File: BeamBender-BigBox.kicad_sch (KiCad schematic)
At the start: 124 parts, among them CN1 A4000-CN621-36, CN2 A4000-CN622-54, J1 HDMI, J2 JTAG, J3 JTAG_Pogo, J4 EXT_BUTTONS, SW1 MENU, SW2 UP, SW3 DOWN, U1 Colorlight-i5-v7.0, U2 TLV76133DCYR, U3 74LVC16244ADGG, U4 74LVC16244ADGG, U5 SII9022ACNU, U6 74LVC1G86, U7 AK5720VT, U8 AP2112K-1.2, X1 Oscillator_3.2x2.5mm-27MHz, X2 Oscillator_5.0x3.2mm_24.576MHz

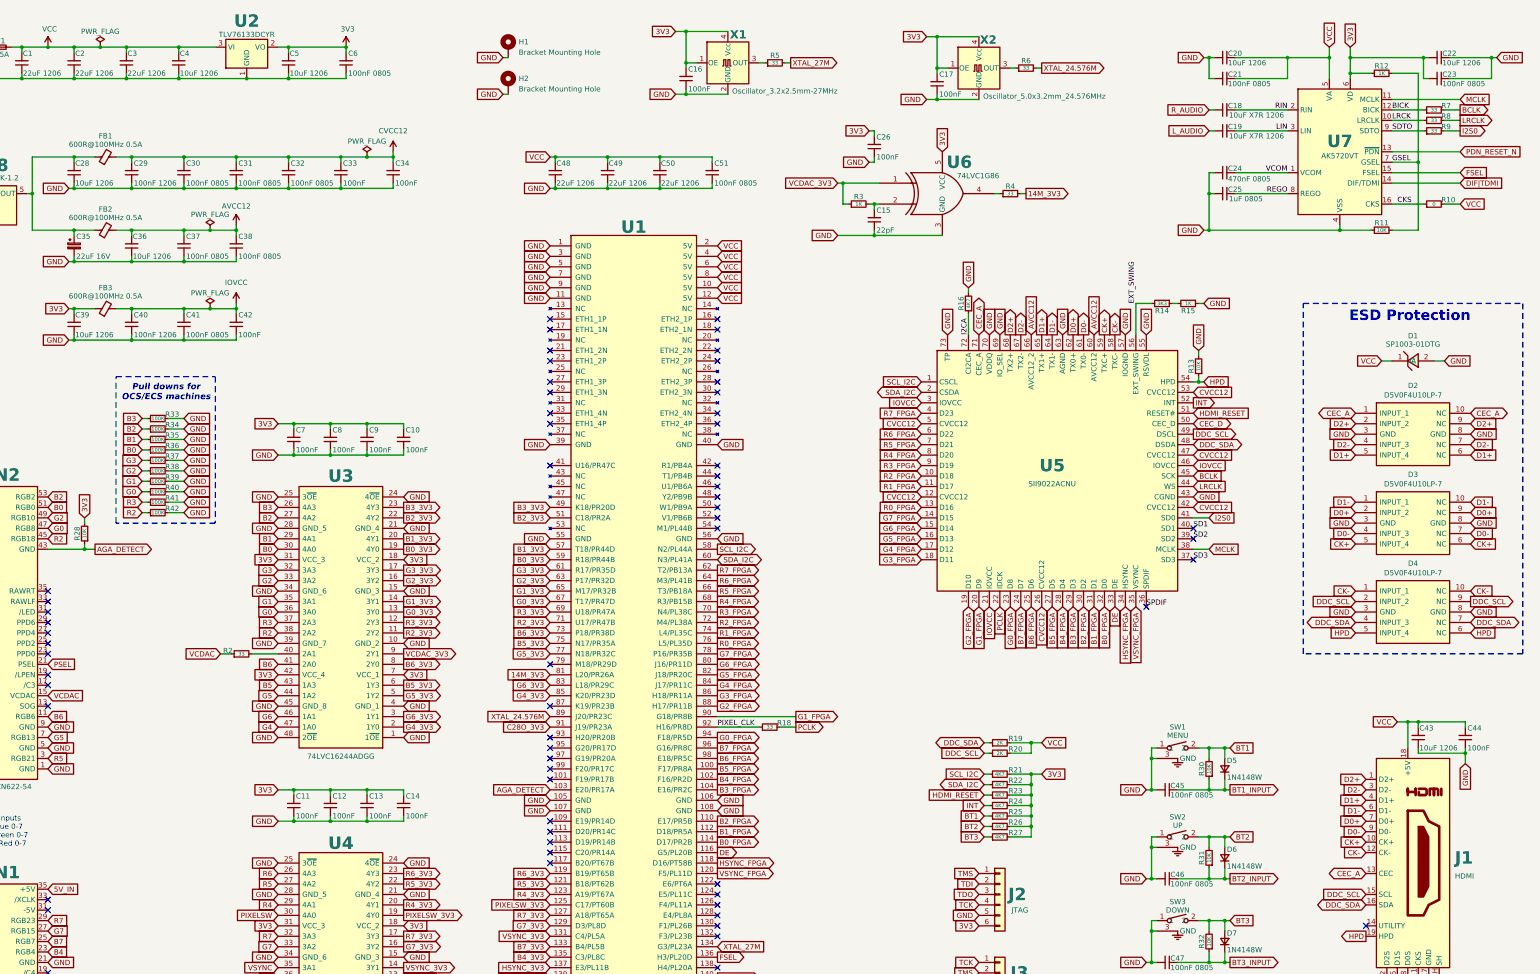
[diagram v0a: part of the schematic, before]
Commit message: Add R0/R1 pull down resistors
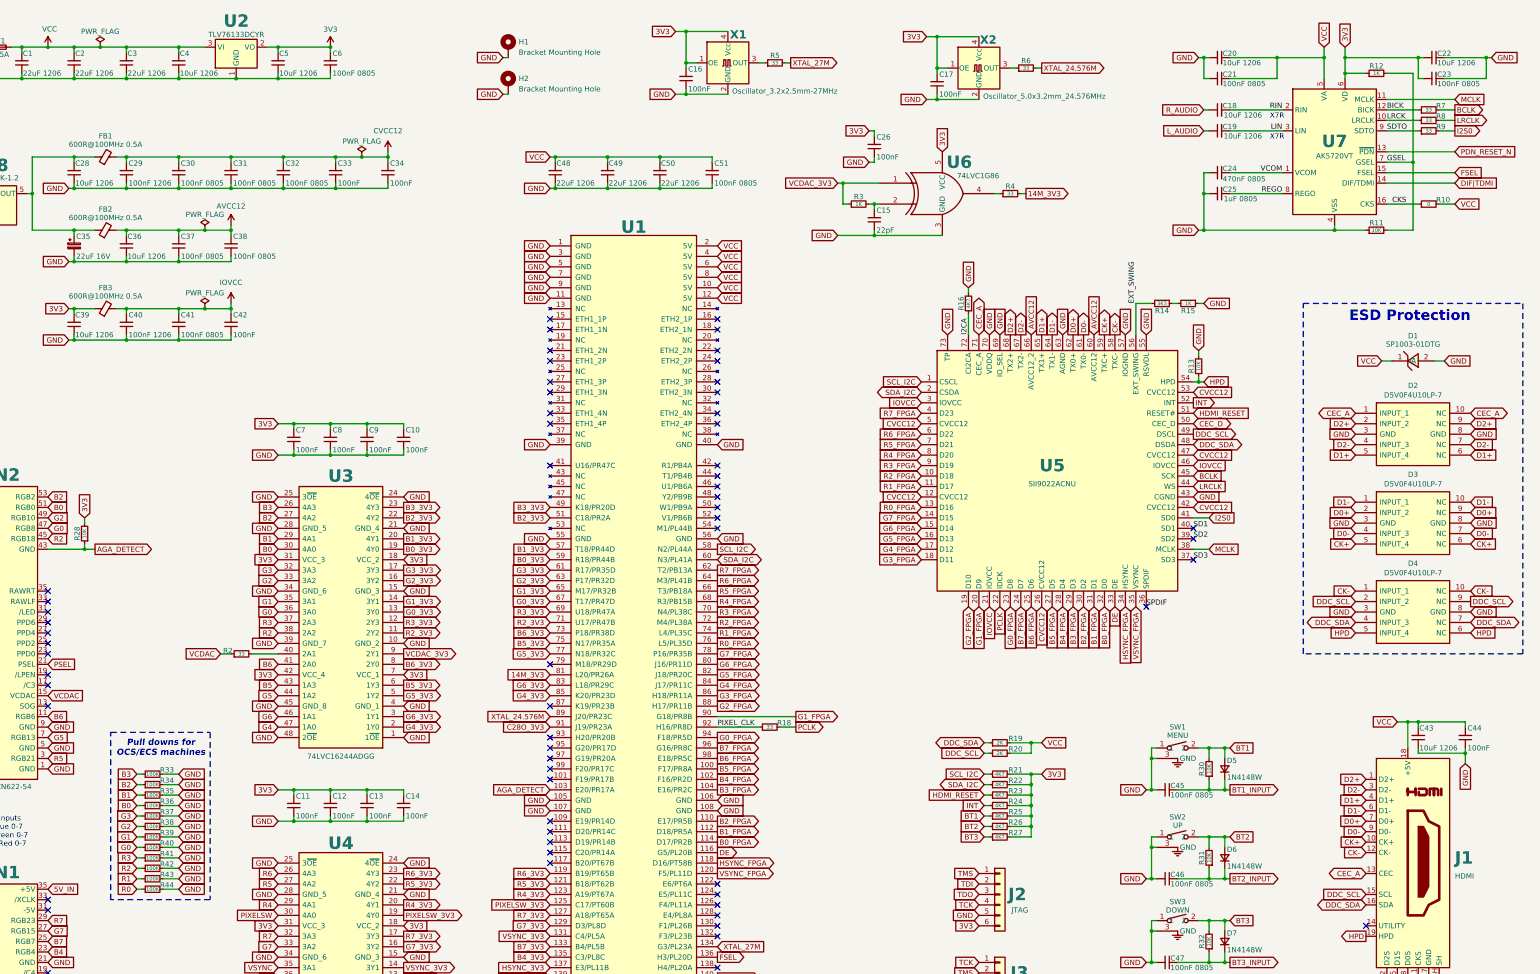
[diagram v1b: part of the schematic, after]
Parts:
- added R43, R44: 100K, Resistor_SMD:R_0603_1608Metric, symbol Device:R_Small
- C1, C2, C3, C48, C49, C50: LCSC C12891 -> C90146; Part Number CL31A226KAHNNNE -> CL31A226KOHNNNE
- C18, C19: value 10uF X7R 1206 -> 10uF 1206; LCSC C97954 -> C96449; Part Number GRM31CR71C106KA12L -> CL31B106KPHNNNE
- C20, C22, C28, C36, C39, C4, C43, C5: LCSC C13585 -> C96449; Part Number CL31A106KBHNNNE -> CL31B106KPHNNNE
- C35: LCSC C242120 -> C445073; Part Number EEEFK1C220R -> UWT1C220MCL1GB
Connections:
- net GND: now also R43.2, R44.2
- net R0: now also R44.1
- net R1: now also R43.1
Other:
- note added: "X7R"
- moved on the sheet: C18, C19, C20, C21, C22, C23, C24, C25, C29, C30, C31, C32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

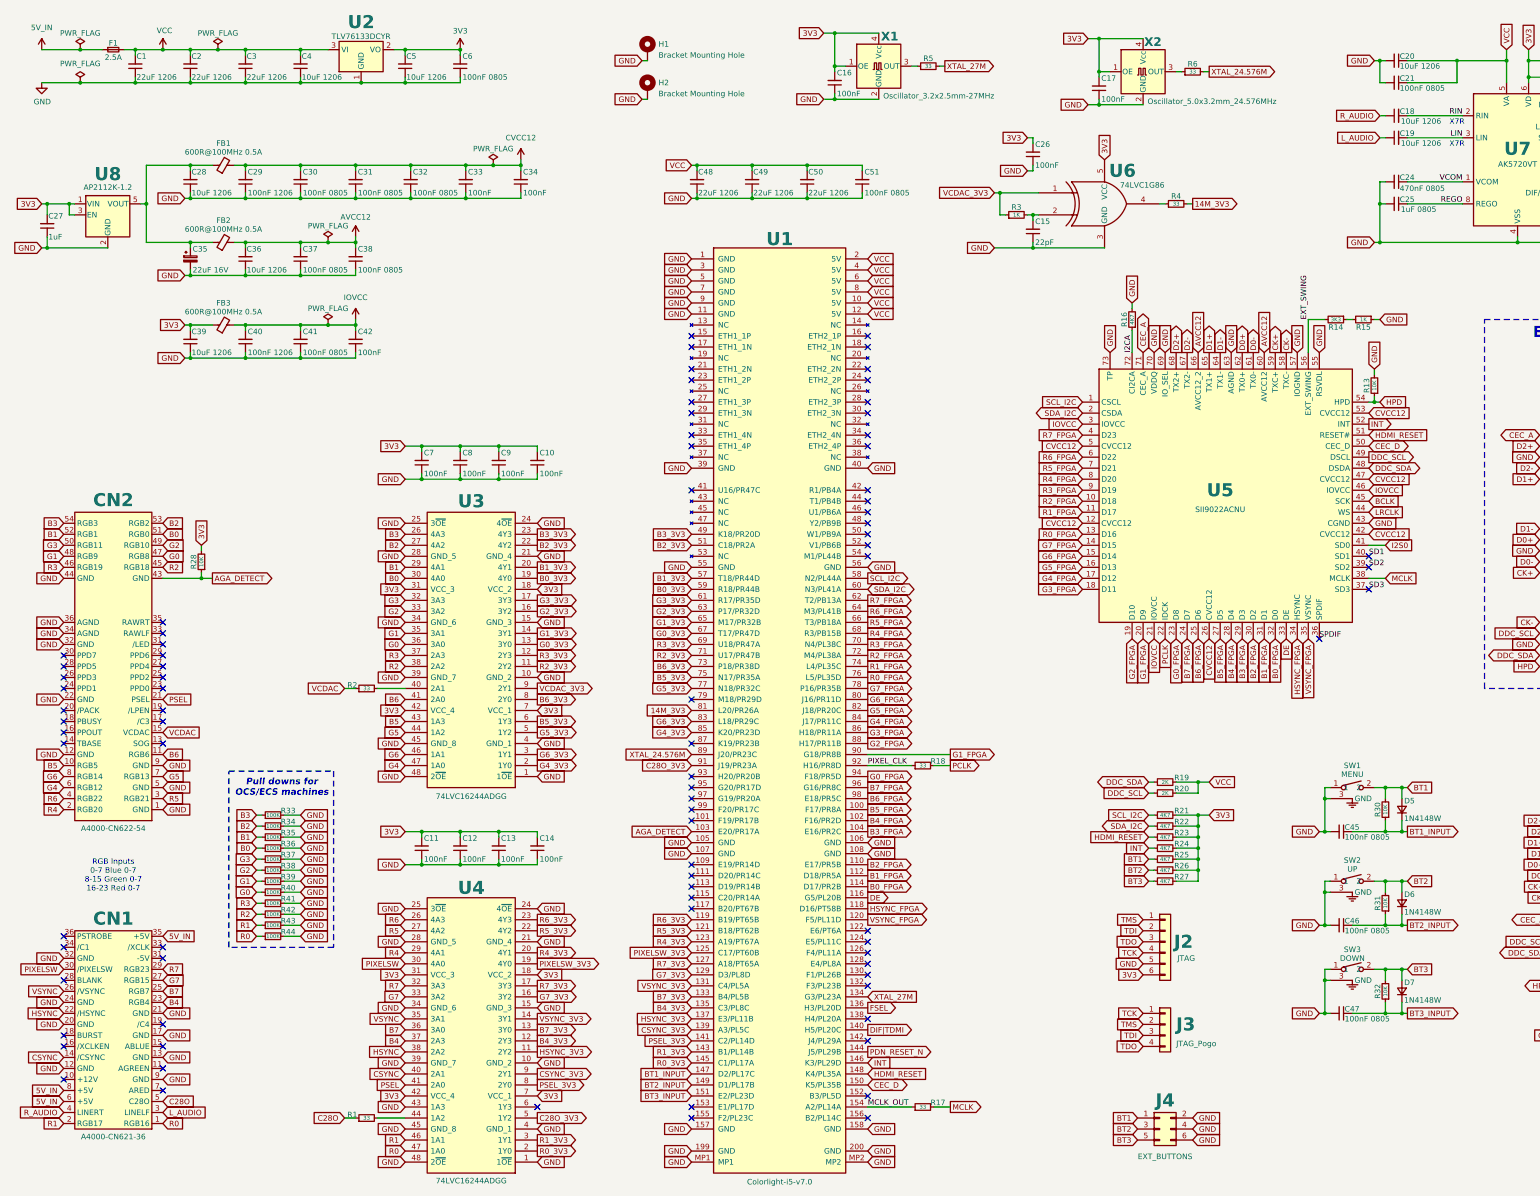
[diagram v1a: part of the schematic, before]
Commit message: Add EXT audio input mixed with Paula audio
External audio input via 3.5mm jack with an alternative 3 pin internal header mixed with Paula audio via OPA1692.
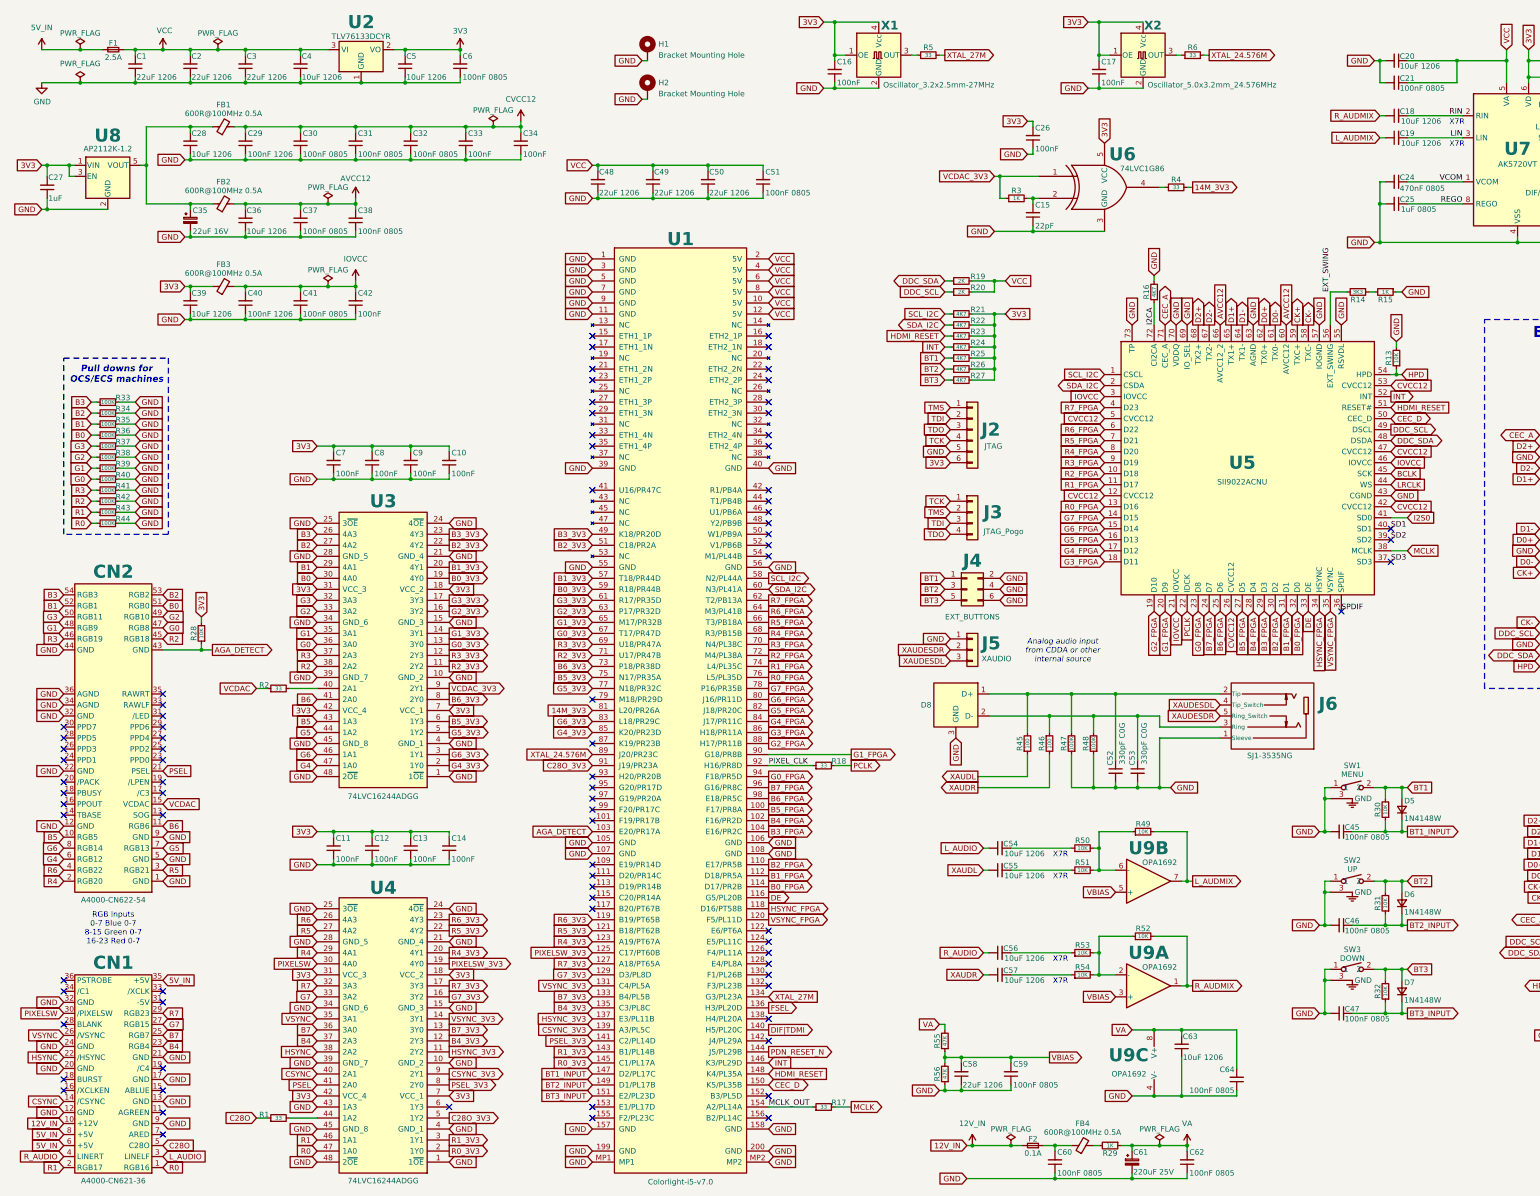
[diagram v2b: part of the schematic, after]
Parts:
- added C52, C53: 330pF C0G, Capacitor_SMD:C_0603_1608Metric, symbol Device:C_Small
- added C54, C55, C56, C57, C63: 10uF 1206, Capacitor_SMD:C_1206_3216Metric, symbol Device:C_Small
- added C58: 22uF 1206, Capacitor_SMD:C_1206_3216Metric, symbol Device:C_Small
- added C59, C60, C62, C64: 100nF 0805, Capacitor_SMD:C_0805_2012Metric, symbol Device:C_Small
- added C61: 220uF 25V, Capacitor_SMD:CP_Elec_6.3x7.7, symbol Device:C_Polarized_Small
- added D8: TPD2E009, Package_TO_SOT_SMD:SOT-23, symbol BeamBenderSymbols:TPD2E009
- added F2: 0.1A, Fuse:Fuse_1206_3216Metric, symbol Device:Fuse_Small
- added FB4: 600R@100MHz 0.5A, Inductor_SMD:L_0805_2012Metric, symbol Device:FerriteBead_Small
- added J5: XAUDIO, Connector_PinHeader_2.54mm:PinHeader_1x03_P2.54mm_Vertical, symbol Connector_Generic:Conn_01x03
- added J6: SJ1-3535NG, BeamBenderFootprints:AUDIO-TH_SJ1-3535NG, symbol BeamBenderSymbols:SJ1-3535NG
- added R29: 1K, Resistor_SMD:R_0603_1608Metric, symbol Device:R_Small
- added R45, R46: 100, Resistor_SMD:R_0603_1608Metric, symbol Device:R_Small
- added R47, R48: 100K, Resistor_SMD:R_0603_1608Metric, symbol Device:R_Small
- added R49, R50, R51, R52, R53, R54: 10K, Resistor_SMD:R_0603_1608Metric, symbol Device:R_Small
- added R55, R56: 47K, Resistor_SMD:R_0603_1608Metric, symbol Device:R_Small
- added U9: OPA1692, Package_SO:SOIC-8_3.9x4.9mm_P1.27mm, symbol Amplifier_Operational:OPA1692xD
- C1, C2, C3, C48, C49, C50: MPN (none) -> CL31A226KOHNNNE; Part Number CL31A226KOHNNNE -> (none)
- C10, C11, C12, C13, C14, C16, C17, C26, C33, C34, C42, C44, C7, C8, C9: MPN (none) -> CC0603KRX7R9BB104; Part Number CC0603KRX7R9BB104 -> (none)
- C15: MPN (none) -> CL10C220JB8NNNC; Part Number CL10C220JB8NNNC -> (none)
- C18, C19, C20, C22, C28, C36, C39, C4, C43, C5: MPN (none) -> CL31B106KPHNNNE; Part Number CL31B106KPHNNNE -> (none)
- C21, C23, C30, C31, C32, C37, C38, C41, C45, C46, C47, C51, C6: MPN (none) -> CL21B104KCFNNNE; Part Number CL21B104KCFNNNE -> (none)
- C24: MPN (none) -> CL21B474KBFNNNE; Part Number CL21B474KBFNNNE -> (none)
- C25: MPN (none) -> CL21B105KBFNNNE; Part Number CL21B105KBFNNNE -> (none)
- C27: MPN (none) -> CL10A105KB8NNNC; Part Number CL10A105KB8NNNC -> (none)
- C29, C40: MPN (none) -> CL31B104KBCNNNC; Part Number CL31B104KBCNNNC -> (none)
- C35: MPN (none) -> UWT1C220MCL1GB; Part Number UWT1C220MCL1GB -> (none)
- D1: MPN (none) -> SP1003-01DTG; Part Number SP1003-01DTG -> (none)
- D2, D3, D4: MPN (none) -> D5V0F4U10LP-7; Part Number D5V0F4U10LP-7 -> (none)
- D5, D6, D7: MPN (none) -> 1N4148W; Part Number 1N4148W -> (none)
- F1: MPN (none) -> 1206L250/16AR; Part Number 1206L250/16AR -> (none)
- FB1, FB2, FB3: MPN (none) -> GZ2012D601TF; Part Number GZ2012D601TF -> (none)
- J1: MPN (none) -> HDMI-001 19PCBTP; Part Number HDMI-001 19PCBTP -> (none)
- J2: MPN (none) -> HB-PH3-25416PB2GOP; Part Number HB-PH3-25416PB2GOP -> (none)
- J4: MPN (none) -> 2541WV-2x03P; Part Number 2541WV-2x03P -> (none)
- R1, R17, R18, R2, R4, R5, R6, R7, R8, R9: MPN (none) -> 0603WAF330JT5E; Part Number 0603WAF330JT5E -> (none)
- R10: MPN (none) -> 0603WAF0000T5E; Part Number 0603WAF0000T5E -> (none)
- R11, R13, R28, R30, R31, R32: MPN (none) -> 0603WAF1002T5E; Part Number 0603WAF1002T5E -> (none)
- R12, R15, R3: MPN (none) -> 0603WAF1001T5E; Part Number 0603WAF1001T5E -> (none)
- R14: MPN (none) -> 0603WAF3301T5E; Part Number 0603WAF3301T5E -> (none)
- R16, R21, R22, R23, R24, R25, R26, R27: MPN (none) -> 0603WAF4701T5E; Part Number 0603WAF4701T5E -> (none)
- R19, R20: MPN (none) -> 0603WAF2001T5E; Part Number 0603WAF2001T5E -> (none)
- R33, R34, R35, R36, R37, R38, R39, R40, R41, R42, R43, R44: MPN (none) -> 0603WAF1003T5E; Part Number 0603WAF1003T5E -> (none)
- SW1, SW2, SW3: MPN (none) -> TS-1038-A10B3-D2; Part Number TS-1038-A10B3-D2 -> (none)
- U1: MPN (none) -> 1473149-4; Part Number 1473149-4 -> (none)
- U2: MPN (none) -> TLV76133DCYR; Part Number TLV76133DCYR -> (none)
- U3, U4: MPN (none) -> 74LVC16244ADGG,118; Part Number 74LVC16244ADGG,118 -> (none)
- U5: MPN (none) -> SII9022ACNU; Part Number SII9022ACNU -> (none)
- U6: MPN (none) -> SN74LVC1G86DBVR; Part Number SN74LVC1G86DBVR -> (none)
- U7: MPN (none) -> AK5720VT; Part Number AK5720VT -> (none)
- U8: MPN (none) -> AP2112K-1.2TRG1; Part Number AP2112K-1.2TRG1 -> (none)
- X1: MPN (none) -> XOS32027000LT00351005; Part Number XOS32027000LT00351005 -> (none)
- X2: MPN (none) -> SX5M24.576M20F30TNN; Part Number SX5M24.576M20F30TNN -> (none)
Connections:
- net GND: now also C52.2, C53.2, C58.1, C59.1, C60.1, C61.2, C62.1, C63.1, C64.1, D8.3 (GND), J5.1 (Pin_1), J6.1 (Sleeve), R47.1, R48.1, R56.1, U9.4 (V-)
- net L_AUDIO: now also C54.1; no longer C19.1
- net R_AUDIO: now also C56.1; no longer C18.1
- net 12V_IN: now reaches CN1.10 (+12V)
- net 12V_IN: now also F2.2
- new net: C55.2, R51.1
- new net: C56.2, R53.1
- new net: R52.1, R53.2, R54.2, U9.2 (-)
- new net: C52.1, D8.1 (D+), J6.2 (Tip), R45.2, R47.2
- new net: C60.2, F2.1, FB4.1
- new net: C53.1, D8.2 (D-), J6.3 (Ring), R46.1, R48.2
- new net: FB4.2, R29.2
- new net: C54.2, R50.1
- new net: R49.1, R50.2, R51.2, U9.6 (-)
- new net: C57.2, R54.1
- new net L_AUDMIX: C19.1, R49.2, U9.7
- new net R_AUDMIX: C18.1, R52.2, U9.1
- new net VA: C61.1, C62.2, C63.2, C64.2, R29.1, R55.2, U9.8 (V+)
- new net VBIAS: C58.2, C59.2, R55.1, R56.2, U9.3 (+), U9.5 (+)
- new net XAUDESDL: J5.3 (Pin_3), J6.4 (Tip_Switch)
- new net XAUDESDR: J5.2 (Pin_2), J6.5 (Ring_Switch)
- new net XAUDL: C55.1, R45.1
- new net XAUDR: C57.1, R46.2
- no-connect marks 84 -> 83
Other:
- note added: "Analog audio input from CDDA or other internal source"
- moved on the sheet: C10, C11, C12, C13, C14, C15, C16, C17, C26, C27, C28, C29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
